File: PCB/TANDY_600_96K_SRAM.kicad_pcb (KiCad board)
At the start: 2 copper layers, 68.6 x 45.1 mm, 9 parts, among them P1 DIN 41612 44P male horiz, U1 128k x 8 5v SRAM, U2 74HC08, U3 74HC148

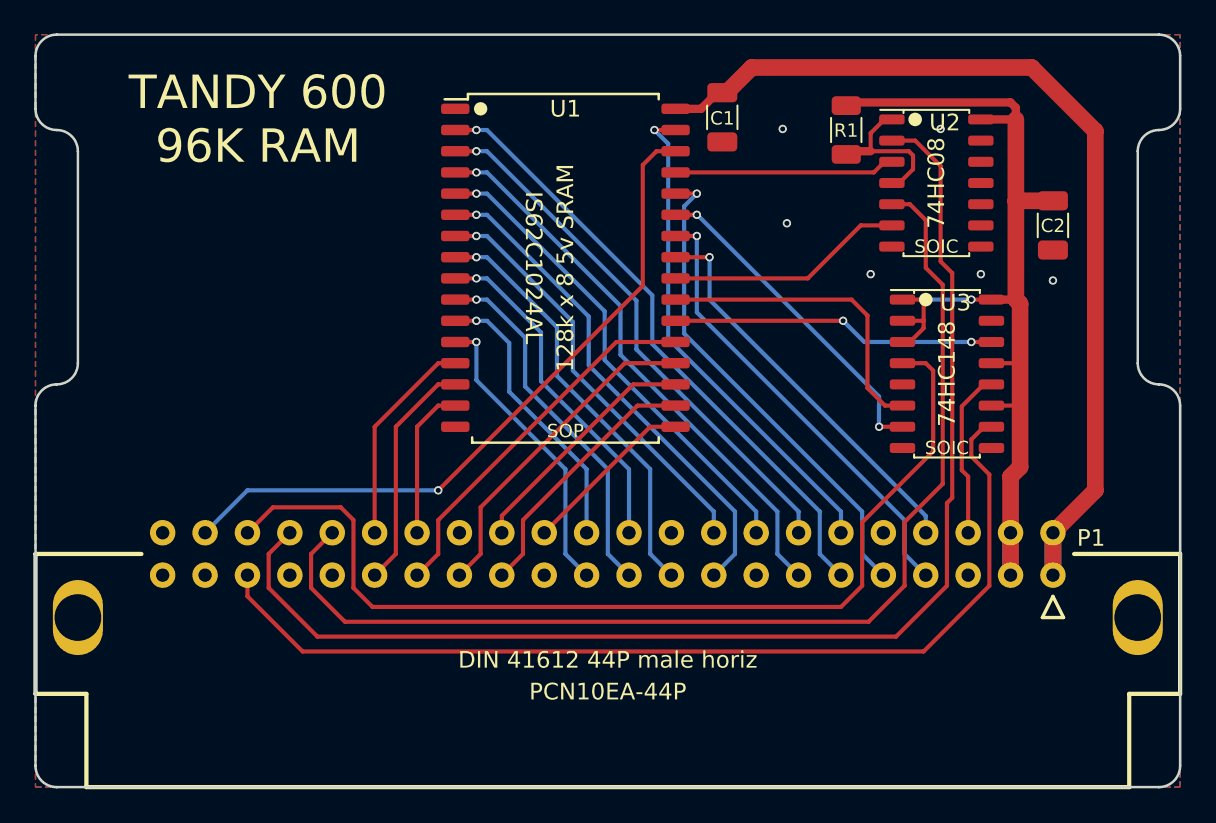
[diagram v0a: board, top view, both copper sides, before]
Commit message: remove 74HC08
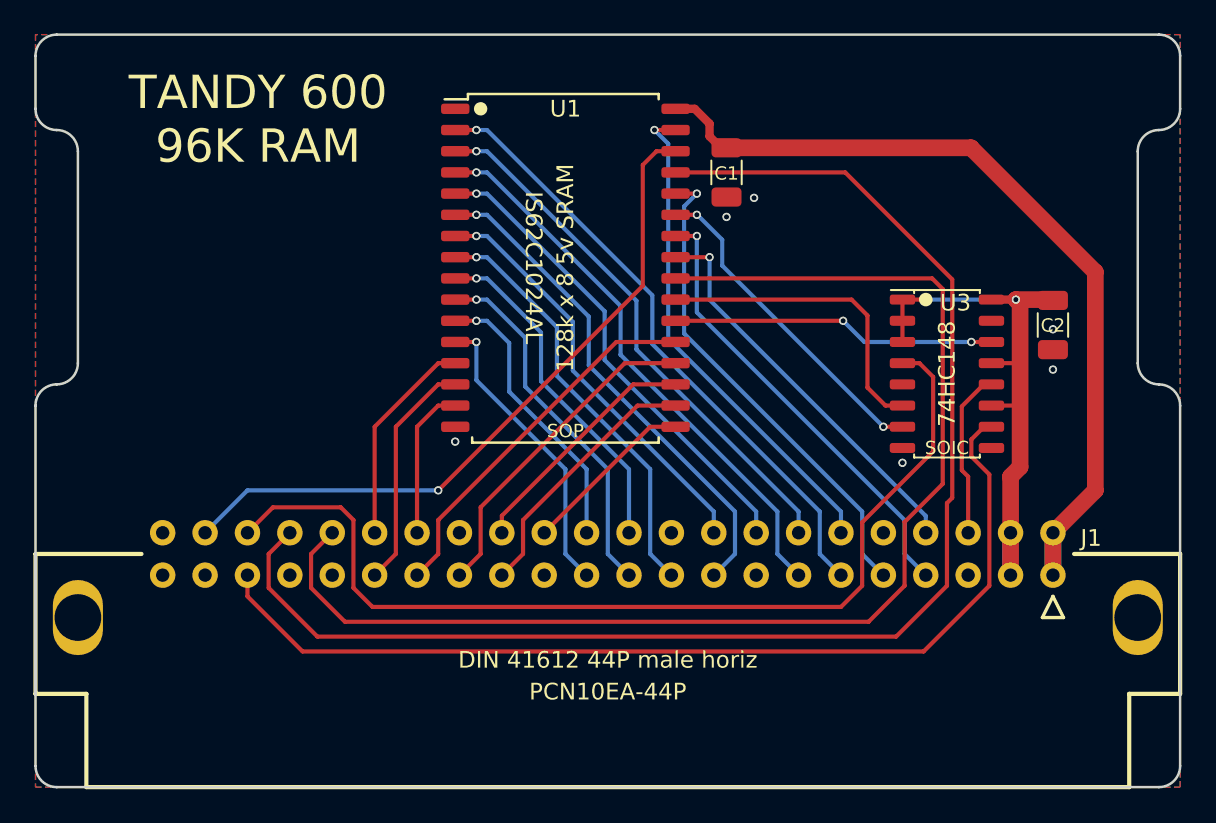
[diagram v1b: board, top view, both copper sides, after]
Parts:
- removed R1: 10K, 000_LOCAL:R_1206
- removed U2: 74HC08, 000_LOCAL:SOIC-14_4x9
- moved C2 5.97 mm to (172.7, 109.5)
- moved C1 3.31 mm to (153.2, 100.3)
- renumbered P1 to J1
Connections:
- U1 pad 24: /~OE~_Gated -> /~OE
- U1 pad 29: /~WE~_Gated -> /~WE
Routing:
- net VCC: track 60.5 -> 37.3 mm
- net /~OE~_Gated: track 14.2 -> 0.00 mm
- net /~WE~_Gated: track 13.2 -> 0.00 mm
- net /PU: track 9.95 -> 0.00 mm
- net /~OE: track 66.9 -> 76.1 mm
- net /~WE: track 76.7 -> 85.3 mm
- net VMEM: track 58.0 -> 51.4 mm
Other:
- board text added: "Based on Model600Sram_v1.1 by Jayeson Lee-Steere"
- board text added: "v003"
- board text removed: "Public Domain design originally by Jayeson Lee-Steere"
- board text removed: "v002"

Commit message: re-order the signal lines so they match from bus to chip
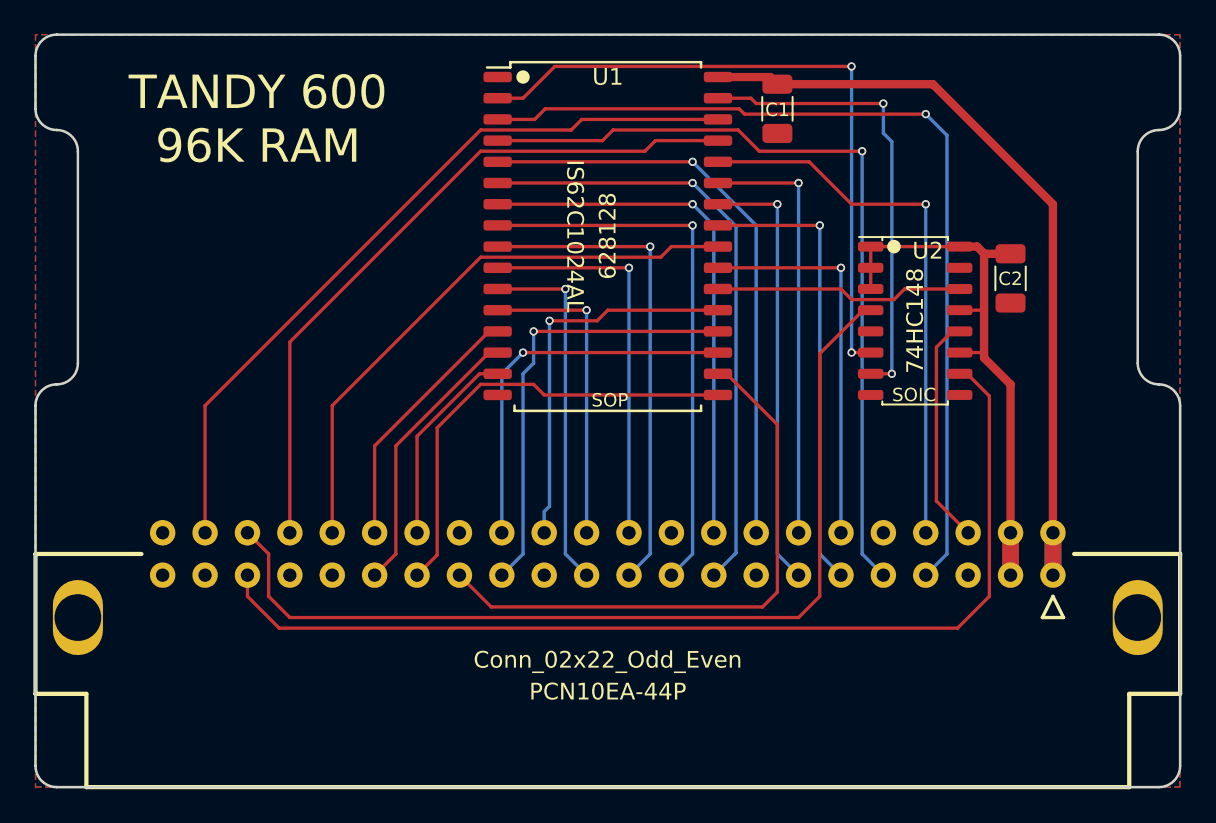
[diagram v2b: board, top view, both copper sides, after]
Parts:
- removed U3: 74HC148, 000_LOCAL:SOIC-16_4x10
- added U2: 74HC148, 000_LOCAL:SOIC-16_4x10, F.Cu at (164.5, 109.2)
- J1: value DIN 41612 44P male horiz -> Conn_02x22_Odd_Even
- U1: value 128k x 8 5v SRAM -> 628128
- moved C1 4.88 mm to (156.2, 96.5)
- moved C2 3.78 mm to (170.2, 106.7)
- moved U1 3.18 mm to (146.1, 104.1)
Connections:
- J1 pad 39: /~CS1~_Bank2 -> /~CS_B2
- J1 pad 40: /~CS1~_Bank1 -> /~CS_B1
- J1 pad 6: /~CS1~_Bank0 -> /~CS_B0
- U1 pad 10: /A3 -> /A2
- U1 pad 11: /A0 -> /A1
- U1 pad 12: /A1 -> /A0
- U1 pad 17: /D7 -> /D3
- U1 pad 18: /D6 -> /D4
- U1 pad 2: /A11 -> /A16
- U1 pad 20: /D4 -> /D6
- U1 pad 21: /D3 -> /D7
- U1 pad 22: /CS1 -> /~CS1
- U1 pad 23: /A16 -> /A10
- U1 pad 25: /A13 -> /A11
- U1 pad 26: /A14 -> /A9
- U1 pad 27: /A15 -> /A8
- U1 pad 28: /A12 -> /A13
- U1 pad 3: /A8 -> /A14
- U1 pad 31: /A10 -> /A15
- U1 pad 4: /A9 -> /A12
- U1 pad 9: /A2 -> /A3
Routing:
- net /~CS_B2: track 0.00 -> 61.6 mm
- net /~CS1~_Bank2: track 59.5 -> 0.00 mm
- net /~CS1~_Bank1: track 59.3 -> 0.00 mm
- net /~CS_B1: track 0.00 -> 57.1 mm
- net /~WE: track 85.3 -> 42.7 mm
- net /~OE: track 76.1 -> 34.7 mm
- net /A14: track 27.3 -> 54.7 mm
- net /A16: track 18.7 -> 40.3 mm, vias 0 -> 2
- net /CS1: track 19.5 -> 0.00 mm, vias 2 -> 0
- net /A12: track 29.4 -> 48.6 mm
- net /D4: track 19.8 -> 35.1 mm
- net /~CS1: track 0.00 -> 15.0 mm
- net /~CS_B0: track 0.00 -> 13.7 mm
- net /D7: track 10.5 -> 23.2 mm, vias 0 -> 1
- net /D6: track 15.8 -> 26.4 mm, vias 0 -> 1
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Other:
- board text added: "v004"
- board text removed: "v003"

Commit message: move chip away from edge, add service manual scans
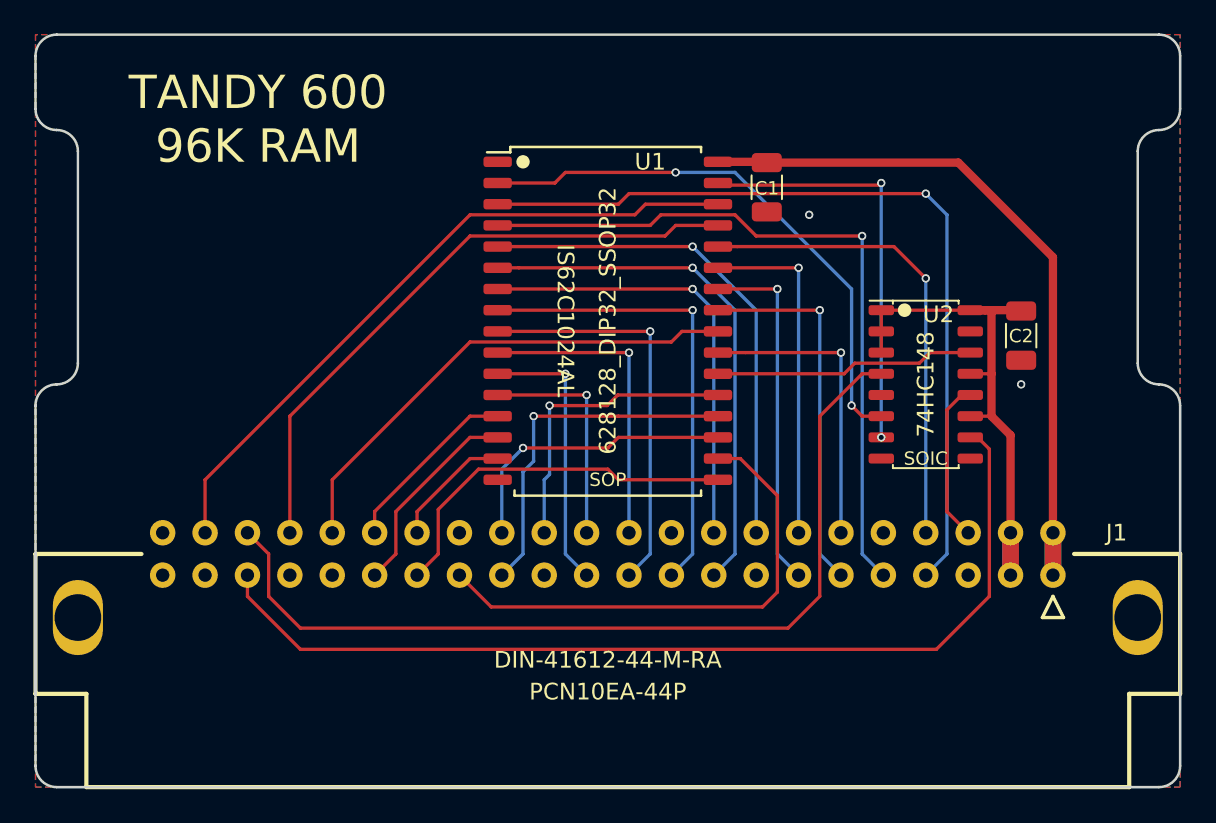
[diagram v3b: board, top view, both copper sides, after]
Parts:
- J1: value Conn_02x22_Odd_Even -> DIN-41612-44-M-RA
- U1: value 628128 -> 628128_DIP32_SSOP32
- moved U1 5.08 mm to (146.1, 109.2)
- moved C1 4.74 mm to (155.6, 101.2)
- moved U2 3.86 mm to (165.1, 113.0)
- moved C2 3.49 mm to (170.8, 110.1)
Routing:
- net /A16: track 40.3 -> 33.4 mm
- net /D5: track 23.0 -> 17.5 mm
- net /A6: track 36.8 -> 31.7 mm
- net /A0: track 18.7 -> 13.6 mm
- net /A7: track 35.5 -> 30.4 mm
- net /D7: track 23.2 -> 18.1 mm
- net /D6: track 26.4 -> 21.4 mm
- net /A9: track 26.3 -> 21.2 mm
- net /A8: track 25.8 -> 20.7 mm
- net /A5: track 31.9 -> 26.8 mm
- net /A3: track 29.4 -> 24.3 mm
- net /A2: track 23.7 -> 18.7 mm
- net /A11: track 27.6 -> 22.5 mm
- net /A10: track 23.2 -> 18.2 mm
- net /A1: track 21.7 -> 16.7 mm
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
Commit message: support either SOIC or SOP 74HC148
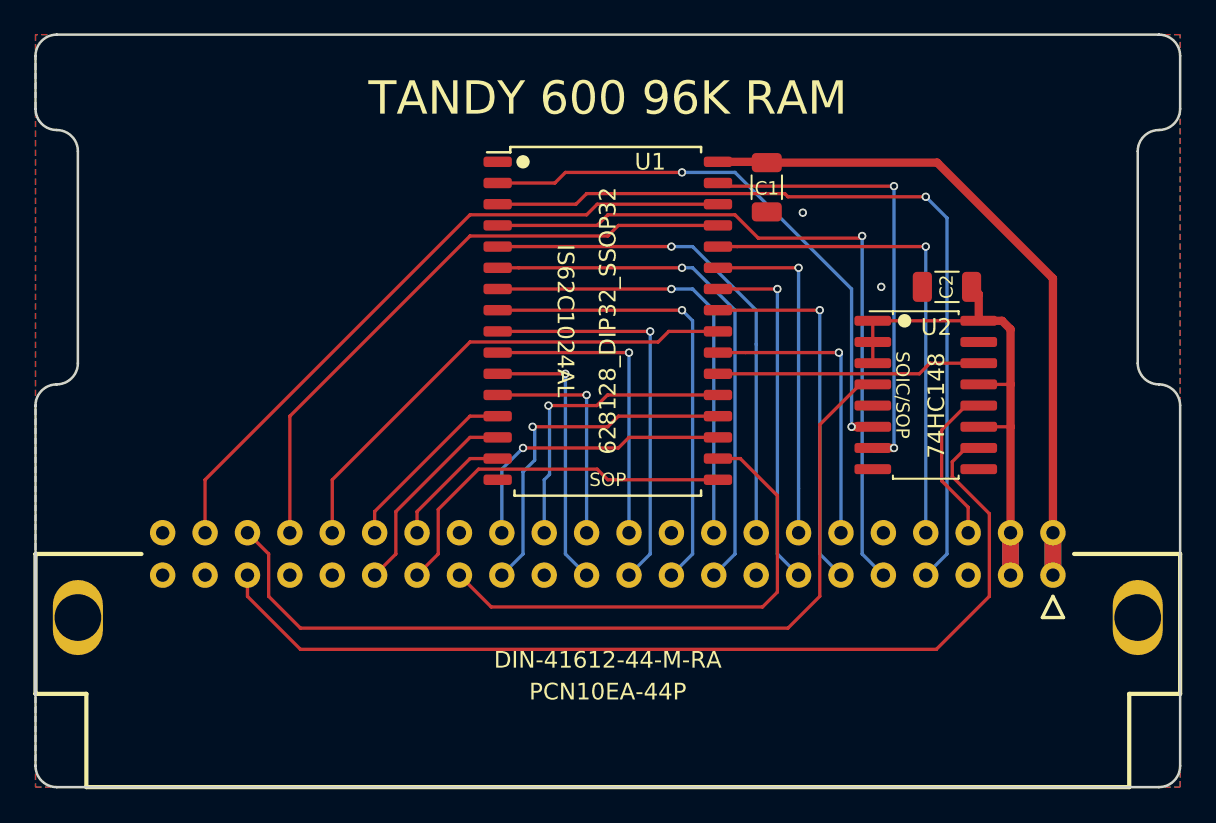
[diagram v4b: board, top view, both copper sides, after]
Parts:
- U2: footprint 000_LOCAL:SOIC-16_4x10 -> 000_LOCAL:SOIC-SOP-16
- moved C2 5.32 mm to (166.4, 107.2), turned to 180 degrees
- moved U2 0.64 mm to (165.1, 113.7)
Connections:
- net /~CS_B0 renamed /~CS1_A
- net /~CS_B1 renamed /~CS1_B
- net /~CS_B2 renamed /~CS1_C
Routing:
- net /A15: track 25.1 -> 27.6 mm
- net /A13: track 28.5 -> 29.6 mm
- net /~CS1_B: track 54.5 -> 53.4 mm
- net VMEM: track 44.0 -> 43.3 mm
- net VCC: track 33.6 -> 34.3 mm
- net /~CS1_C: track 58.6 -> 59.3 mm
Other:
- board text added: "Case contact points"
- board text added: "Originally based on Model600Sram_v1.1 by Jayeson Lee-Steere"
- board text added: "SOIC/SOP"
- board text added: "b.kenyon.w@gmail.com"
- board text added: "github.com/bkw777/TANDY_600_RAM v005"
- board text added: "~CS1_A~"
- board text added: "~CS1_B~"
- board text added: "~CS1_C~"
- board text removed: "Based on Model600Sram_v1.1 by Jayeson Lee-Steere"
- board text removed: "SOIC"
- board text removed: "This height is specific and functional. The top of the case prevents the cards from falling out."
- board text removed: "github.com/bkw777/TANDY_600_RAM"
- board text removed: "v004"
- board text removed: "~CS1~ Bank 0"
- board text removed: "~CS1~ Bank 1"
- board text removed: "~CS1~ Bank 2"

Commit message: unscramble cs_a,b,c -> a15,16
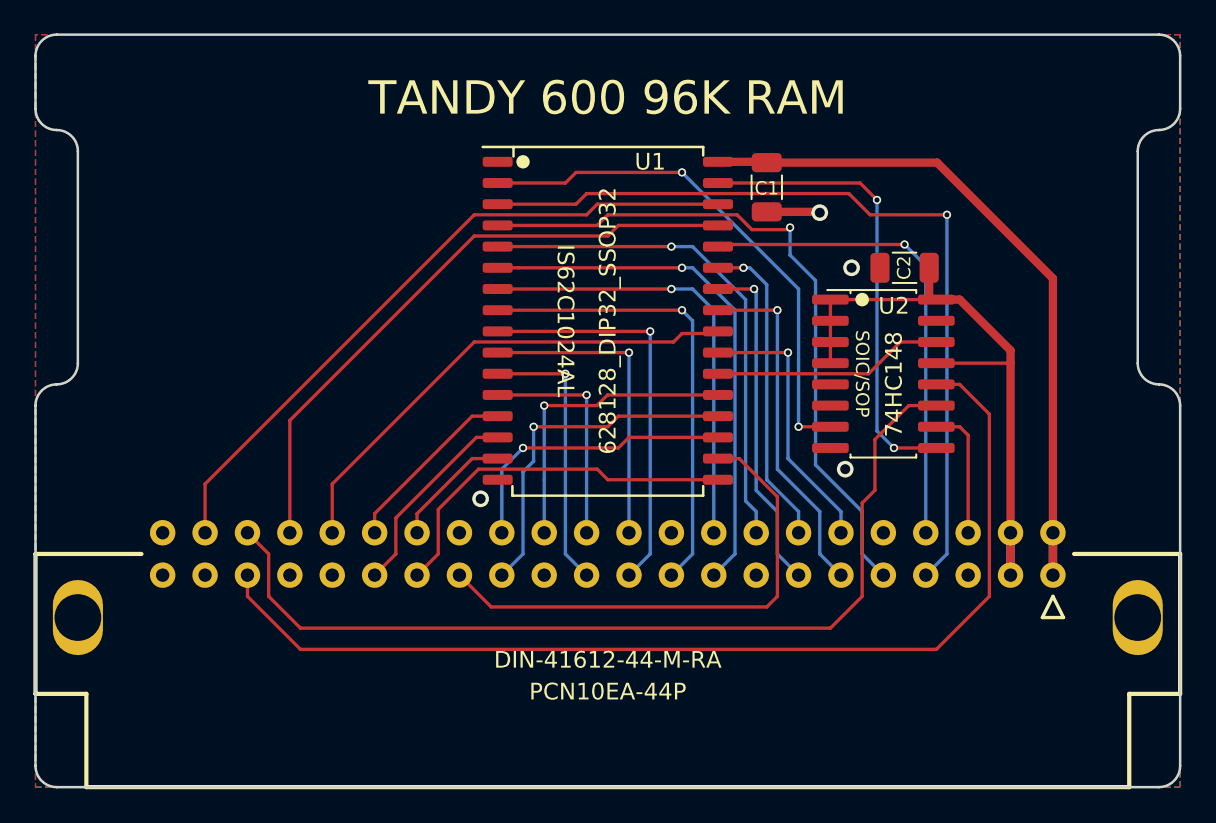
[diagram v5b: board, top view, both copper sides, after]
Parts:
- moved U2 2.84 mm to (162.6, 112.4)
- moved C2 2.79 mm to (163.8, 106.0)
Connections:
- U2 pad 10: /~CS1_C -> /~CS1_A
- U2 pad 11: VCC -> /~CS1_B
- U2 pad 12: /~CS1_A -> /~CS1_C
- U2 pad 4: /~CS1_B -> VCC
- U2 pad 6: /A16 -> (no net)
- U2 pad 7: /A15 -> /A16
- U2 pad 9: (no net) -> /A15
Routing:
- net VCC: track 34.3 -> 38.7 mm
- net /~CS1_C: track 59.3 -> 63.2 mm
- net GND: track 0.00 -> 3.20 mm, vias 2 -> 4
- net /A16: track 33.9 -> 31.3 mm
- net /~CS1_B: track 53.4 -> 55.7 mm
- net /A12: track 43.6 -> 41.3 mm
- net /~CS1: track 15.9 -> 13.9 mm
- net /A10: track 18.1 -> 16.3 mm
- net /A8: track 20.7 -> 19.0 mm
- net /~CS1_A: track 9.64 -> 7.96 mm
- net /A11: track 22.5 -> 21.0 mm
- net /A9: track 21.2 -> 20.4 mm
- net /A13: track 29.6 -> 29.0 mm
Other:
- board text added: "github.com/bkw777/TANDY_600_RAM v006"
- board text removed: "SOP"
- board text removed: "github.com/bkw777/TANDY_600_RAM v005"

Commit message: v006.1
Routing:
- net VCC: track 38.7 -> 36.4 mm
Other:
- board text added: "96K RAM for TANDY 600"
- board text removed: "TANDY 600 96K RAM"
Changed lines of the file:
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@@
-(kicad_pcb (version 20171130) (host pcbnew 5.1.10-88a1d61d58~88~ubuntu20.10.1)
+(kicad_pcb (version 20171130) (host pcbnew 5.1.10-88a1d61d58~90~ubuntu21.04.1)
   (general
     (thickness 1.6)
     (drawings 89)
-    (tracks 212)
+    (tracks 213)
     (zones 0)
     (modules 7)
@@
       (effects (font (size 1 1) (thickness 0.15)))
     )
-    (fp_text user %R (at 0 -0.635) (layer F.Fab)
-      (effects (font (size 0.98 0.98) (thickness 0.15)))
-    )
     (fp_circle (center -1.27 -4.445) (end -1.0668 -4.445) (layer F.SilkS) (width 0.4064))
     (fp_line (start -1.9685 -4.826) (end -1.9685 -5.0165) (layer F.SilkS) (width 0.12))
@@
     (fp_line (start 3.7 5.215) (end 3.7 -5.215) (layer F.CrtYd) (width 0.05))
     (fp_line (start 3.7 -5.215) (end -3.7 -5.215) (layer F.CrtYd) (width 0.05))
+    (fp_text user %R (at 0 -0.635) (layer F.Fab)
+      (effects (font (size 0.98 0.98) (thickness 0.15)))
+    )
     (pad 5 smd roundrect (at -3.1735 0.635) (size 2.2 0.6) (layers F.Cu F.Paste F.Mask) (roundrect_rratio 0.25)
       (net 1 GND))
@@
       (effects (font (size 1 1) (thickness 0.15)))
     )
-    (fp_text user %R (at 1.905 0 -90) (layer F.Fab)
-      (effects (font (size 1 1) (thickness 0.12)))
-    )
     (fp_line (start -5.715 10.4775) (end -5.715 9.906) (layer F.SilkS) (width 0.15))
     (fp_line (start 5.715 9.906) (end 5.715 10.4775) (layer F.SilkS) (width 0.15))
@@
     (fp_line (start 5.715 -10.414) (end 5.715 -9.906) (layer F.SilkS) (width 0.15))
     (fp_line (start -5.6515 -9.8425) (end -5.6515 -10.414) (layer F.SilkS) (width 0.15))
+    (fp_text user %R (at 1.905 0 -90) (layer F.Fab)
+      (effects (font (size 1 1) (thickness 0.12)))
+    )
     (pad 26 smd roundrect (at 6.6 -1.905) (size 1.8 0.6) (layers F.Cu F.Paste F.Mask) (roundrect_rratio 0.25)
       (net 9 /A9))
@@
     (effects (font (size 1 1) (thickness 0.15)) (justify left mirror))
   )
-  (gr_text "TANDY 600 96K RAM" (at 146.05 95.885) (layer F.SilkS)
+  (gr_text "96K RAM for TANDY 600" (at 146.05 95.885) (layer F.SilkS)
     (effects (font (size 2 2) (thickness 0.3)))
   )
@@
   (segment (start 159.3865 111.76) (end 159.3865 107.9515) (width 0.2) (layer F.Cu) (net 3))
   (segment (start 159.385 107.95) (end 165.7335 107.95) (width 0.2) (layer F.Cu) (net 3))
-  (segment (start 165.7335 111.76) (end 170.18 111.76) (width 0.2) (layer F.Cu) (net 3))
-  (segment (start 170.18 111.76) (end 170.18 121.92) (width 0.5) (layer F.Cu) (net 3))
   (segment (start 165.305 107.95) (end 165.7335 107.95) (width 0.5) (layer F.Cu) (net 3))
   (segment (start 165.305 106.045) (end 165.305 107.95) (width 0.5) (layer F.Cu) (net 3))
-  (segment (start 170.18 110.998) (end 170.18 111.76) (width 0.5) (layer F.Cu) (net 3))
-  (segment (start 167.132 107.95) (end 170.18 110.998) (width 0.5) (layer F.Cu) (net 3))
+  (segment (start 170.18 113.9825) (end 170.18 121.92) (width 0.5) (layer F.Cu) (net 3))
+  (segment (start 167.9575 111.76) (end 170.18 113.9825) (width 0.5) (layer F.Cu) (net 3))
+  (segment (start 167.9575 108.7755) (end 167.9575 111.76) (width 0.5) (layer F.Cu) (net 3))
+  (segment (start 167.132 107.95) (end 167.9575 108.7755) (width 0.5) (layer F.Cu) (net 3))
   (segment (start 165.7335 107.95) (end 167.132 107.95) (width 0.5) (layer F.Cu) (net 3))
+  (segment (start 165.7335 111.76) (end 167.9575 111.76) (width 0.2) (layer F.Cu) (net 3))
   (segment (start 144.145 102.235) (end 139.45 102.235) (width 0.2) (layer F.Cu) (net 4))
   (segment (start 144.78 101.6) (end 144.145 102.235) (width 0.2) (layer F.Cu) (net 4))

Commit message: kicad 6
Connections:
- net /~CS1 renamed /~{CS1}
- net /~CS1_A renamed /~{CS1_A}
- net /~CS1_B renamed /~{CS1_B}
- net /~CS1_C renamed /~{CS1_C}
- net /~OE renamed /~{OE}
- net /~WE renamed /~{WE}
- J1 pad : (no net) -> GND
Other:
- net class Default removed
- board text added: "${COMMENT2} v${REVISION}"
- board text added: "Top cover actual contact points and elevation."
- board text added: "~{CS1_A}"
- board text added: "~{CS1_B}"
- board text added: "~{CS1_C}"
- board text added: "~{OE}"
- board text added: "~{WE}"
- board text removed: "Case contact points"
- board text removed: "b.kenyon.w@gmail.com"
- board text removed: "github.com/bkw777/TANDY_600_RAM v006"
- board text removed: "~CS1_A~"
- board text removed: "~CS1_B~"
- board text removed: "~CS1_C~"
- board text removed: "~OE"
- board text removed: "~WE"
